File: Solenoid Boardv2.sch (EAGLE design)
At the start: 52 parts, among them Y2 ECS-80-S-4X

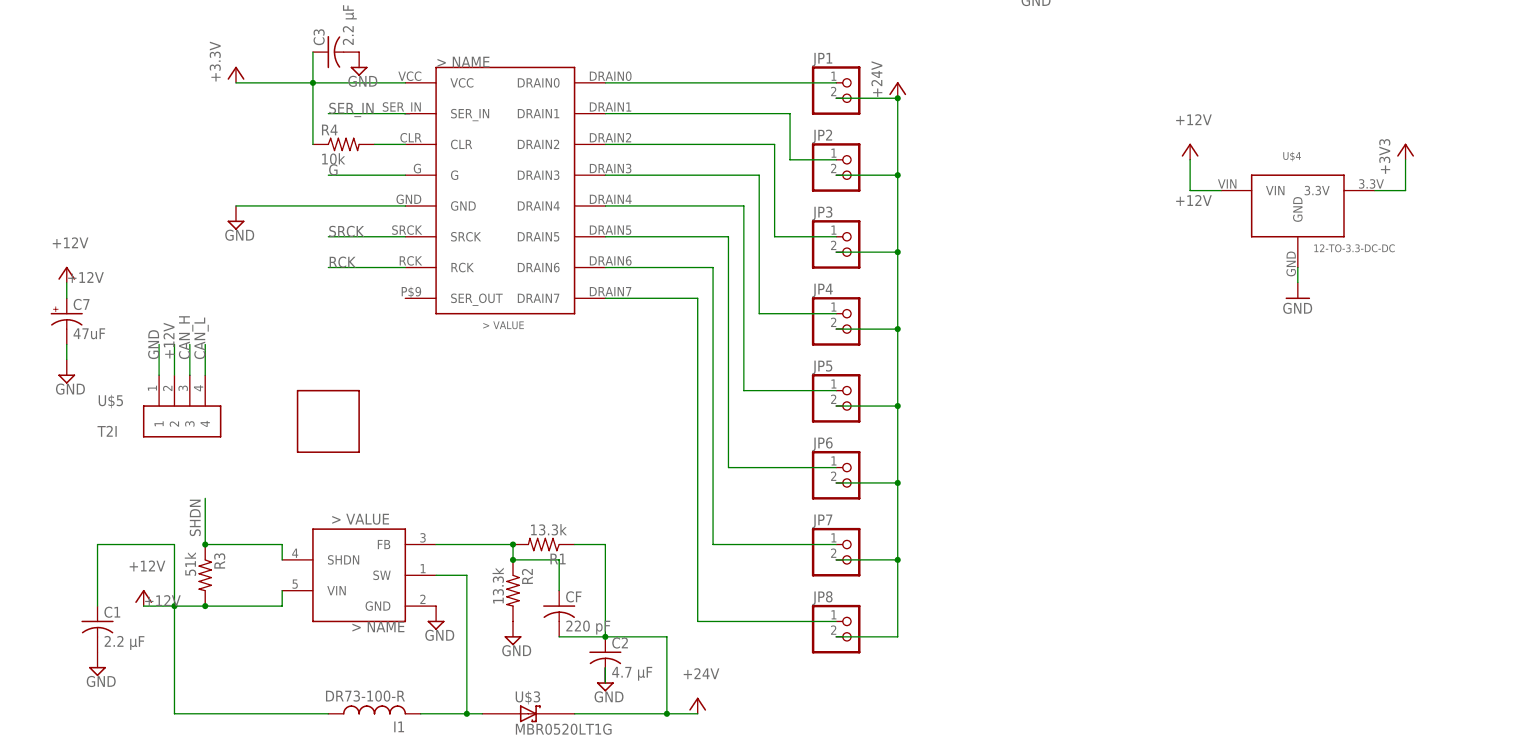
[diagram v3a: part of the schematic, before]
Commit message: WIP changing route widths
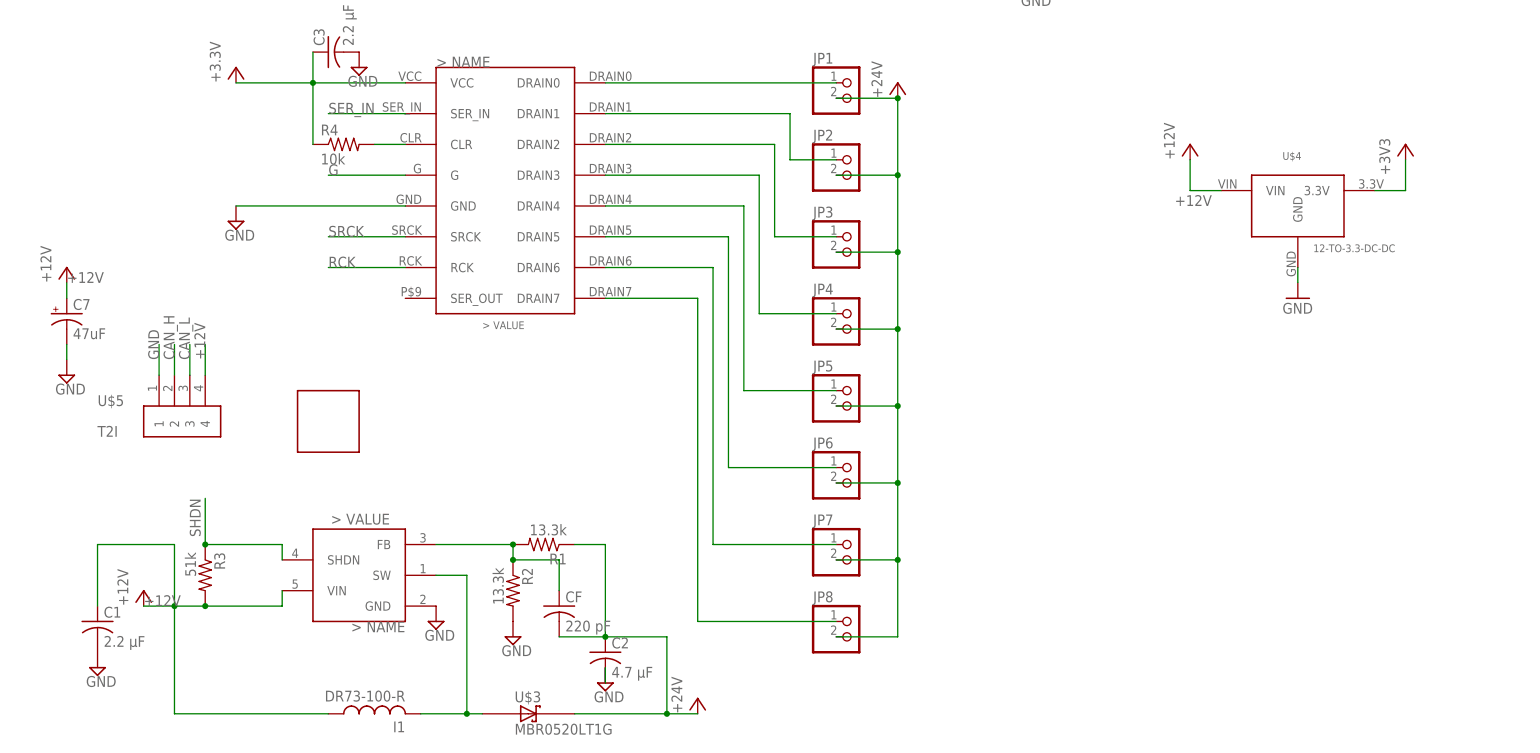
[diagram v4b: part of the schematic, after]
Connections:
- net +12V: now also U$5.4; no longer U$5.2
- net CAN_H: now also U$5.2; no longer U$5.3
- net CAN_L: now also U$5.3; no longer U$5.4
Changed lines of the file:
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@@
 <?xml version="1.0" encoding="utf-8"?>
 <!DOCTYPE eagle SYSTEM "eagle.dtd">
-<eagle version="9.1.3">
+<eagle version="9.2.0">
 <drawing>
 <settings>
@@
 </instance>
 <instance part="+12V" gate="VCC" x="30.48" y="40.64">
-<attribute name="VALUE" x="27.94" y="43.815" size="1.778" layer="96"/>
+<attribute name="VALUE" x="27.94" y="38.1" size="1.778" layer="96" rot="R90"/>
 </instance>
 <instance part="24V" gate="VCC" x="121.92" y="22.86">
-<attribute name="VALUE" x="119.38" y="26.035" size="1.778" layer="96"/>
+<attribute name="VALUE" x="119.38" y="20.32" size="1.778" layer="96" rot="R90"/>
 </instance>
 <instance part="SUPPLY8" gate="GND" x="45.72" y="101.6">
@@
 <attribute name="VALUE" x="175.26" y="137.16" size="1.778" layer="96"/>
 </instance>
-<instance part="U$4" gate="A" x="220.98" y="101.6"/>
+<instance part="U$4" gate="A" x="220.98" y="101.6">
+<attribute name="NAME" x="218.44" y="111.76" size="1.27" layer="95"/>
+<attribute name="VALUE" x="223.52" y="96.52" size="1.27" layer="95"/>
+</instance>
 <instance part="GND13" gate="1" x="220.98" y="88.9">
 <attribute name="VALUE" x="218.44" y="86.36" size="1.778" layer="96"/>
@@
 </instance>
 <instance part="+12V1" gate="VCC" x="203.2" y="114.3">
-<attribute name="VALUE" x="200.66" y="117.475" size="1.778" layer="96"/>
-</instance>
-<instance part="C7" gate="G$1" x="17.78" y="86.36"/>
+<attribute name="VALUE" x="200.66" y="111.76" size="1.778" layer="96" rot="R90"/>
+</instance>
+<instance part="C7" gate="G$1" x="17.78" y="86.36">
+<attribute name="NAME" x="18.796" y="86.995" size="1.778" layer="95" font="vector"/>
+<attribute name="VALUE" x="18.796" y="82.169" size="1.778" layer="96" font="vector"/>
+</instance>
 <instance part="SUPPLY6" gate="GND" x="17.78" y="76.2">
 <attribute name="VALUE" x="15.875" y="73.025" size="1.778" layer="96"/>
 </instance>
 <instance part="+12V2" gate="VCC" x="17.78" y="93.98">
-<attribute name="VALUE" x="15.24" y="97.155" size="1.778" layer="96"/>
+<attribute name="VALUE" x="15.24" y="91.44" size="1.778" layer="96" rot="R90"/>
 </instance>
 <instance part="H1" gate="G$1" x="10.16" y="200.66"/>
@@
 <net name="+12V" class="0">
 <segment>
-<pinref part="U$5" gate="G$1" pin="2"/>
-<wire x1="35.56" y1="76.2" x2="35.56" y2="81.28" width="0.1524" layer="91"/>
-<label x="35.56" y="78.74" size="1.778" layer="95" rot="R90"/>
-</segment>
-<segment>
 <pinref part="U$2" gate="G$1" pin="VIN"/>
 <wire x1="53.34" y1="40.64" x2="53.34" y2="38.1" width="0.1524" layer="91"/>
@@
 <wire x1="17.78" y1="91.44" x2="17.78" y2="88.9" width="0.1524" layer="91"/>
 <label x="17.78" y="91.44" size="1.778" layer="95"/>
+</segment>
+<segment>
+<pinref part="U$5" gate="G$1" pin="4"/>
+<wire x1="40.64" y1="76.2" x2="40.64" y2="81.28" width="0.1524" layer="91"/>
+<label x="40.64" y="78.74" size="1.778" layer="95" rot="R90"/>
 </segment>
 </net>
@@
 <net name="CAN_H" class="0">
 <segment>
-<pinref part="U$5" gate="G$1" pin="3"/>
-<wire x1="38.1" y1="76.2" x2="38.1" y2="81.28" width="0.1524" layer="91"/>
-<label x="38.1" y="78.74" size="1.778" layer="95" rot="R90"/>
-</segment>
-<segment>
 <pinref part="U$8" gate="G$1" pin="CANH"/>
 <wire x1="137.16" y1="170.18" x2="154.94" y2="170.18" width="0.1524" layer="91"/>
@@
 <wire x1="195.58" y1="177.8" x2="228.6" y2="177.8" width="0.1524" layer="91"/>
 </segment>
+<segment>
+<pinref part="U$5" gate="G$1" pin="2"/>
+<wire x1="35.56" y1="76.2" x2="35.56" y2="81.28" width="0.1524" layer="91"/>
+<label x="35.56" y="78.74" size="1.778" layer="95" rot="R90"/>
+</segment>
 </net>
 <net name="CAN_L" class="0">
-<segment>
-<pinref part="U$5" gate="G$1" pin="4"/>
-<wire x1="40.64" y1="76.2" x2="40.64" y2="81.28" width="0.1524" layer="91"/>
-<label x="40.64" y="78.74" size="1.778" layer="95" rot="R90"/>
-</segment>
 <segment>
 <pinref part="U$8" gate="G$1" pin="CANL"/>
@@
 <wire x1="195.58" y1="147.32" x2="228.6" y2="147.32" width="0.1524" layer="91"/>
 </segment>
-</net>
+<segment>
+<pinref part="U$5" gate="G$1" pin="3"/>
+<wire x1="38.1" y1="76.2" x2="38.1" y2="81.28" width="0.1524" layer="91"/>
+<label x="38.1" y="78.74" size="1.778" layer="95" rot="R90"/>
+</segment>
+</net>

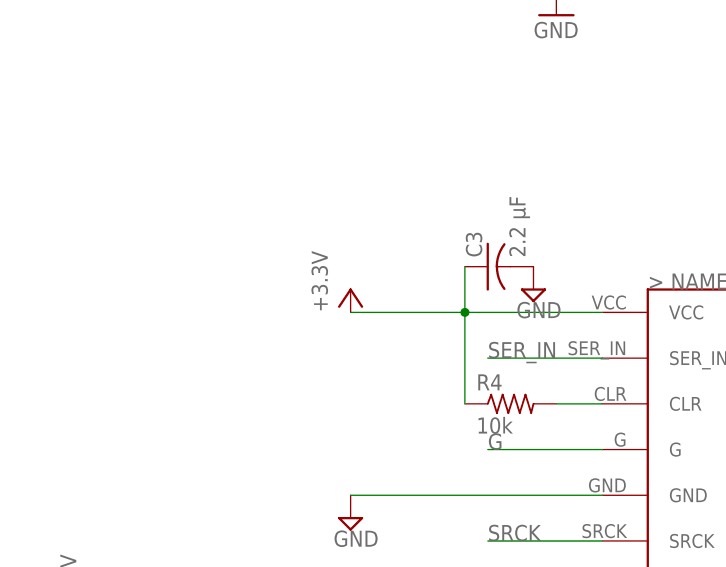
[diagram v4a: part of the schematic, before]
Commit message: Grant's revisions. Detailed in notes.txt
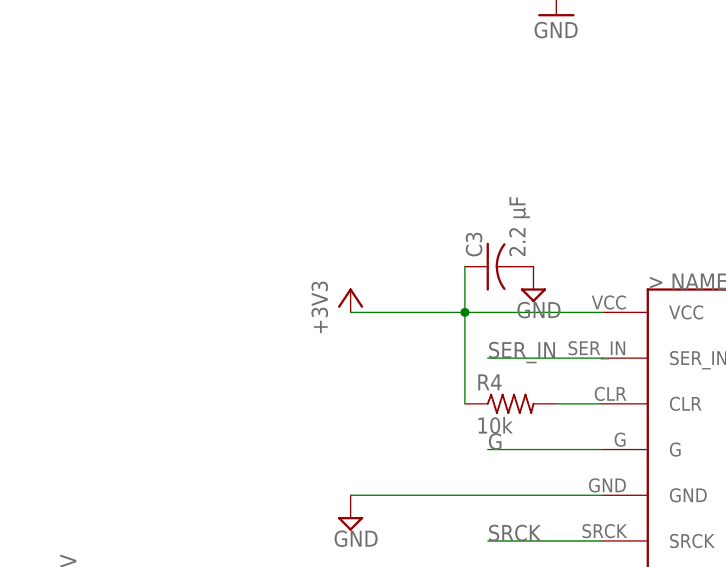
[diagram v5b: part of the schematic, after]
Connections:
- removed net +3.3V: C3.1, R4.1, U$1.VCC
- net +3V3: now also C3.1, R4.1, U$1.VCC
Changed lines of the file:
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@@
 <?xml version="1.0" encoding="utf-8"?>
 <!DOCTYPE eagle SYSTEM "eagle.dtd">
-<eagle version="9.2.0">
+<eagle version="9.1.3">
 <drawing>
 <settings>
@@
 <part name="SUPPLY8" library="supply2" library_urn="urn:adsk.eagle:library:372" deviceset="GND" device=""/>
 <part name="+24V" library="supply1" library_urn="urn:adsk.eagle:library:371" deviceset="VCC" device="" value="+24V"/>
-<part name="+3.3V" library="supply1" library_urn="urn:adsk.eagle:library:371" deviceset="VCC" device="" value="+3.3V"/>
 <part name="C3" library="rcl" library_urn="urn:adsk.eagle:library:334" deviceset="C-US" device="C0805" package3d_urn="urn:adsk.eagle:package:23617/2" value="2.2 µF"/>
 <part name="SUPPLY5" library="supply2" library_urn="urn:adsk.eagle:library:372" deviceset="GND" device=""/>
@@
 <part name="H2" library="SparkFun-Hardware" library_urn="urn:adsk.eagle:library:519" deviceset="STAND-OFF" device="" package3d_urn="urn:adsk.eagle:package:38630/1"/>
 <part name="H3" library="SparkFun-Hardware" library_urn="urn:adsk.eagle:library:519" deviceset="STAND-OFF" device="" package3d_urn="urn:adsk.eagle:package:38630/1"/>
+<part name="+3V5" library="supply1" library_urn="urn:adsk.eagle:library:371" deviceset="+3V3" device=""/>
 </parts>
 <sheets>
@@
 <attribute name="VALUE" x="152.4" y="121.92" size="1.778" layer="96" rot="R90"/>
 </instance>
-<instance part="+3.3V" gate="VCC" x="45.72" y="127">
-<attribute name="VALUE" x="43.18" y="124.46" size="1.778" layer="96" rot="R90"/>
-</instance>
 <instance part="C3" gate="G$1" x="60.96" y="129.54" rot="R90">
 <attribute name="NAME" x="60.325" y="130.556" size="1.778" layer="95" rot="R90"/>
@@
 <instance part="H2" gate="G$1" x="10.16" y="198.12"/>
 <instance part="H3" gate="G$1" x="12.7" y="200.66"/>
+<instance part="+3V5" gate="G$1" x="45.72" y="127">
+<attribute name="VALUE" x="43.18" y="121.92" size="1.778" layer="96" rot="R90"/>
+</instance>
 </instances>
 <busses>
@@
 </segment>
 </net>
-<net name="+3.3V" class="0">
-<segment>
-<pinref part="+3.3V" gate="VCC" pin="VCC"/>
-<pinref part="U$1" gate="G$1" pin="VCC"/>
-<wire x1="45.72" y1="124.46" x2="58.42" y2="124.46" width="0.1524" layer="91"/>
-<pinref part="C3" gate="G$1" pin="1"/>
-<wire x1="58.42" y1="124.46" x2="73.66" y2="124.46" width="0.1524" layer="91"/>
-<wire x1="58.42" y1="129.54" x2="58.42" y2="124.46" width="0.1524" layer="91"/>
-<junction x="58.42" y="124.46"/>
-<pinref part="R4" gate="G$1" pin="1"/>
-<wire x1="58.42" y1="114.3" x2="58.42" y2="124.46" width="0.1524" layer="91"/>
-</segment>
-</net>
 <net name="CLR" class="0">
 <segment>
@@
 <pinref part="+3V2" gate="G$1" pin="+3V3"/>
 </segment>
-</net>
+<segment>
+<pinref part="U$1" gate="G$1" pin="VCC"/>
+<wire x1="45.72" y1="124.46" x2="58.42" y2="124.46" width="0.1524" layer="91"/>
+<pinref part="C3" gate="G$1" pin="1"/>
+<wire x1="58.42" y1="124.46" x2="73.66" y2="124.46" width="0.1524" layer="91"/>
+<wire x1="58.42" y1="129.54" x2="58.42" y2="124.46" width="0.1524" layer="91"/>
+<junction x="58.42" y="124.46"/>
+<pinref part="R4" gate="G$1" pin="1"/>
+<wire x1="58.42" y1="114.3" x2="58.42" y2="124.46" width="0.1524" layer="91"/>
+<pinref part="+3V5" gate="G$1" pin="+3V3"/>
+</segment>
+</net>

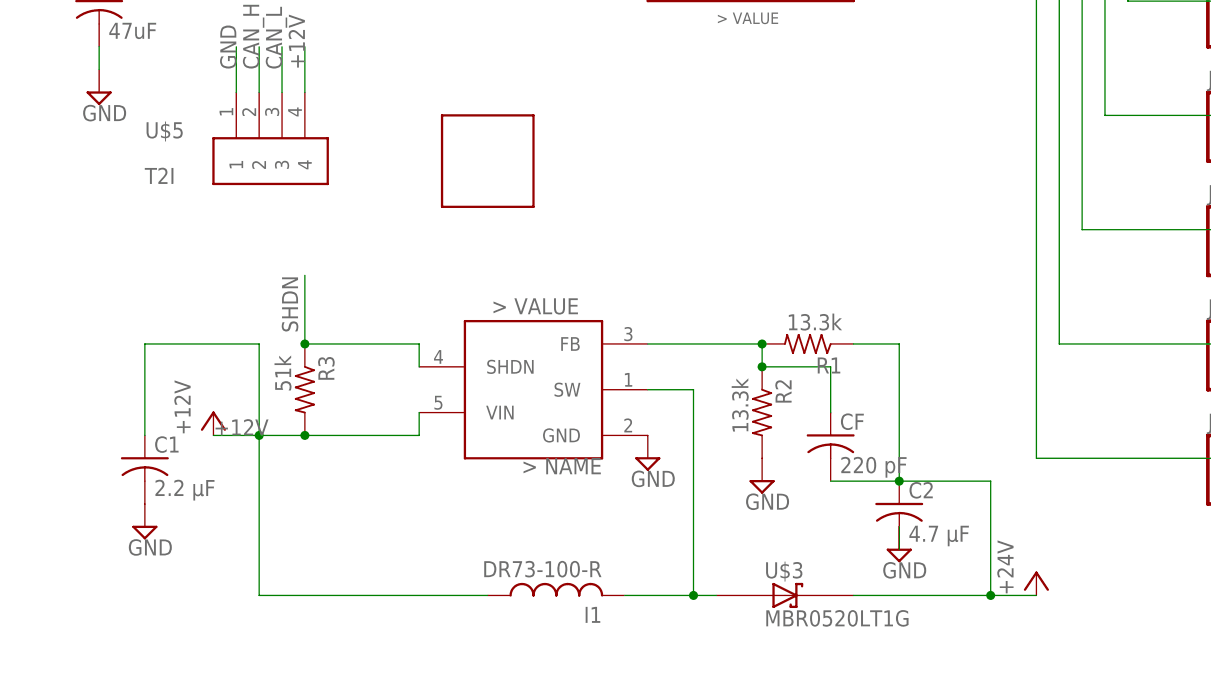
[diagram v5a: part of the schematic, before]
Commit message: revised boost converter resistors and added data sheet for boost converter
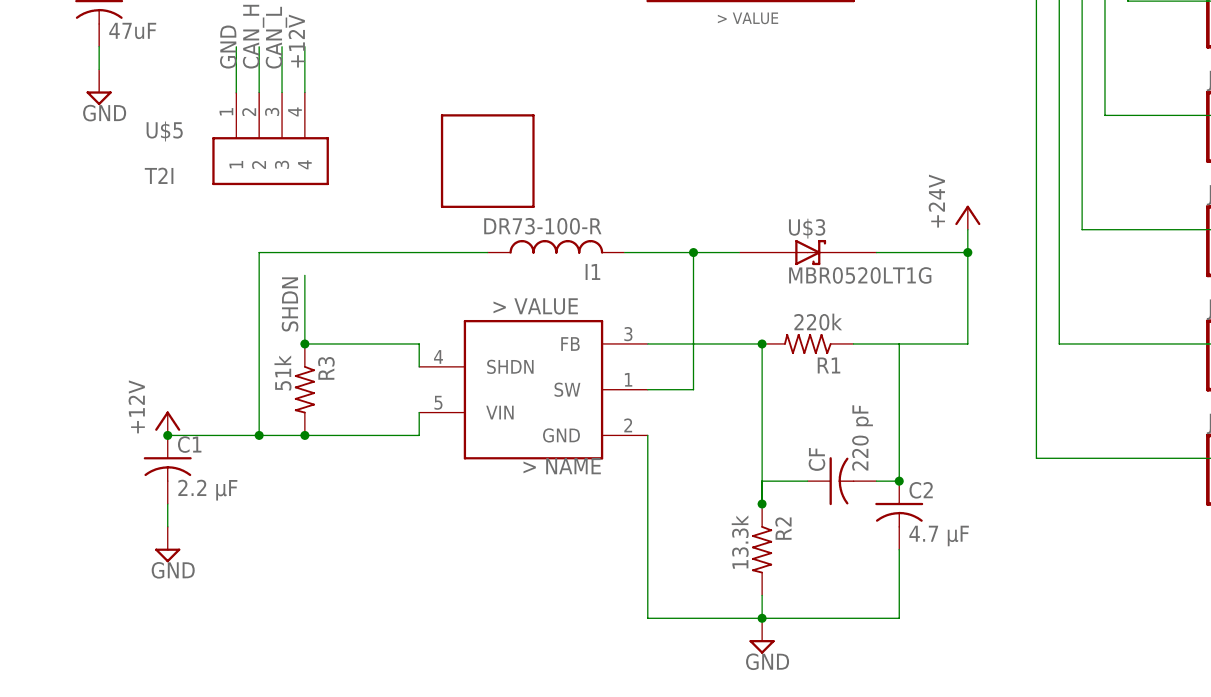
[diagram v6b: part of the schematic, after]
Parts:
- R1: value 13.3k -> 220k
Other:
- moved on the sheet: C1, CF, I1, R2, U$3
